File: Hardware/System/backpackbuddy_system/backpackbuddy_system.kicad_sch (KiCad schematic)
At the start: 27 parts, among them J1 PIR, J2 Ultrasonic 2, J3 Ultrasonic 1, J4 Left Vibration 1, J5 Left Vibration 2, J7 ESP8266, J8 Right Vibration 1, J9 Right Vibration 2, Q1 Q_NMOS_GSD, Q2 Q_NMOS_GSD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

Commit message: almost done
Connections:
- net microcontroller/PB3 is gone; now on net microcontroller/PD0: R10.1
- net +3V3: now also R14.1; no longer SW1.2
- net ESP RESET: now also R14.2; no longer R14.1
- net GND: now also SW1.2; no longer R14.2
- net microcontroller/PD0: no longer J3.3 (Pin_3)
- net microcontroller/PB2 renamed microcontroller/PB7
- net microcontroller/PB6 renamed microcontroller/PD3/TX
- new net microcontroller/PD0: J3.3 (Pin_3)
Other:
- sheet microcontroller ports: added PB7; removed PB2, PB3, PB6
- moved on the sheet: R14, SW1
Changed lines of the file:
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@@
     (stroke (width 0) (type default) (color 0 0 0 0))
   )
-  (wire (pts (xy 245.11 71.12) (xy 245.11 77.47))
+  (wire (pts (xy 245.11 73.66) (xy 245.11 77.47))
     (stroke (width 0) (type default) (color 0 0 0 0))
   )
@@
     (stroke (width 0) (type default) (color 0 0 0 0))
   )
-  (wire (pts (xy 245.11 62.23) (xy 245.11 60.96))
+  (wire (pts (xy 245.11 58.42) (xy 245.11 62.23))
     (stroke (width 0) (type default) (color 0 0 0 0))
   )
@@
     (pin "1")
   )
-  (symbol (lib_id "Switch:SW_Push") (at 245.11 55.88 90) (unit 1)
-    (in_bom yes) (on_board yes) (fields_autoplaced)
-    (property "Reference" "SW1" (id 0) (at 246.38 54.6099 90)
-      (effects (font (size 1.27 1.27)) (justify right))
-    )
-    (property "Value" "ESP8266 RESET" (id 1) (at 246.38 57.1499 90)
-      (effects (font (size 1.27 1.27)) (justify right))
-    )
-    (property "Footprint" "BackpackBuddyFootprintLibrary:RST_SW" (id 2) (at 240.03 55.88 0)
-      (effects (font (size 1.27 1.27)) hide)
-    )
-    (property "Datasheet" "https://www.nkkswitches.com/pdf/HP03-2.pdf" (id 3) (at 240.03 55.88 0)
-      (effects (font (size 1.27 1.27)) hide)
-    )
-    (property "MPN" "HP0315AFKP2-R" (id 4) (at 245.11 55.88 0)
-      (effects (font (size 1.27 1.27)) hide)
-    )
-    (property "Stock" "https://www.digikey.com/en/products/detail/nkk-switches/HP0315AFKP2-R/1242035" (id 5) (at 245.11 55.88 0)
+  (symbol (lib_id "Switch:SW_Push") (at 245.11 68.58 270) (unit 1)
+    (in_bom yes) (on_board yes) (fields_autoplaced)
+    (property "Reference" "SW1" (id 0) (at 248.92 67.3099 90)
+      (effects (font (size 1.27 1.27)) (justify left))
+    )
+    (property "Value" "ESP8266 RESET" (id 1) (at 248.92 69.8499 90)
+      (effects (font (size 1.27 1.27)) (justify left))
+    )
+    (property "Footprint" "BackpackBuddyFootprintLibrary:RST_SW" (id 2) (at 250.19 68.58 0)
+      (effects (font (size 1.27 1.27)) hide)
+    )
+    (property "Datasheet" "https://www.nkkswitches.com/pdf/HP03-2.pdf" (id 3) (at 250.19 68.58 0)
+      (effects (font (size 1.27 1.27)) hide)
+    )
+    (property "MPN" "HP0315AFKP2-R" (id 4) (at 245.11 68.58 0)
+      (effects (font (size 1.27 1.27)) hide)
+    )
+    (property "Stock" "https://www.digikey.com/en/products/detail/nkk-switches/HP0315AFKP2-R/1242035" (id 5) (at 245.11 68.58 0)
       (effects (font (size 1.27 1.27)) hide)
     )
@@
     (pin "1")
   )
-  (symbol (lib_id "Device:R") (at 245.11 67.31 0) (unit 1)
-    (in_bom yes) (on_board yes) (fields_autoplaced)
-    (property "Reference" "R14" (id 0) (at 247.65 66.0399 0)
-      (effects (font (size 1.27 1.27)) (justify left))
-    )
-    (property "Value" "10k" (id 1) (at 247.65 68.5799 0)
-      (effects (font (size 1.27 1.27)) (justify left))
-    )
-    (property "Footprint" "Resistor_SMD:R_0603_1608Metric_Pad0.98x0.95mm_HandSolder" (id 2) (at 243.332 67.31 90)
-      (effects (font (size 1.27 1.27)) hide)
-    )
-    (property "Datasheet" "~" (id 3) (at 245.11 67.31 0)
-      (effects (font (size 1.27 1.27)) hide)
-    )
-    (property "MPN" "RES 10K OHM 1% 1/10W 0603" (id 4) (at 245.11 67.31 0)
-      (effects (font (size 1.27 1.27)) hide)
-    )
-    (property "Stock" "https://www.digikey.com/en/products/detail/vishay-dale/CRCW060310K0FKECC/12744930?utm_adgroup=Resistors&utm_source=google&utm_medium=cpc&utm_campaign=Shopping_Supplier_Vishay&utm_term=&utm_content=Resistors" (id 5) (at 245.11 67.31 0)
+  (symbol (lib_id "Device:R") (at 245.11 54.61 0) (unit 1)
+    (in_bom yes) (on_board yes) (fields_autoplaced)
+    (property "Reference" "R14" (id 0) (at 247.65 53.3399 0)
+      (effects (font (size 1.27 1.27)) (justify left))
+    )
+    (property "Value" "10k" (id 1) (at 247.65 55.8799 0)
+      (effects (font (size 1.27 1.27)) (justify left))
+    )
+    (property "Footprint" "Resistor_SMD:R_0603_1608Metric_Pad0.98x0.95mm_HandSolder" (id 2) (at 243.332 54.61 90)
+      (effects (font (size 1.27 1.27)) hide)
+    )
+    (property "Datasheet" "~" (id 3) (at 245.11 54.61 0)
+      (effects (font (size 1.27 1.27)) hide)
+    )
+    (property "MPN" "RES 10K OHM 1% 1/10W 0603" (id 4) (at 245.11 54.61 0)
+      (effects (font (size 1.27 1.27)) hide)
+    )
+    (property "Stock" "https://www.digikey.com/en/products/detail/vishay-dale/CRCW060310K0FKECC/12744930?utm_adgroup=Resistors&utm_source=google&utm_medium=cpc&utm_campaign=Shopping_Supplier_Vishay&utm_term=&utm_content=Resistors" (id 5) (at 245.11 54.61 0)
       (effects (font (size 1.27 1.27)) hide)
     )
@@
       (effects (font (size 1.27 1.27)) (justify right))
     )
-    (pin "PB2" bidirectional (at 132.08 43.18 180)
+    (pin "PB7" bidirectional (at 132.08 43.18 180)
       (effects (font (size 1.27 1.27)) (justify left))
     )
@@
       (effects (font (size 1.27 1.27)) (justify right))
     )
-    (pin "PB3" bidirectional (at 132.08 58.42 180)
+    (pin "PD0" bidirectional (at 132.08 58.42 180)
       (effects (font (size 1.27 1.27)) (justify left))
     )
@@
       (effects (font (size 1.27 1.27)) (justify left))
     )
-    (pin "PB6" bidirectional (at 132.08 66.04 180)
+    (pin "PD3{slash}TX" bidirectional (at 132.08 66.04 180)
       (effects (font (size 1.27 1.27)) (justify left))
     )
@@
       (reference "C24") (unit 1) (value "10uF") (footprint "Capacitor_SMD:C_0805_2012Metric_Pad1.18x1.45mm_HandSolder")
     )
-    (path "/b75bd9b9-3a6b-4766-98aa-3c30f703f2e0/a43d5dce-b543-4961-b95c-4a978a724427"
-      (reference "C25") (unit 1) (value "10uF") (footprint "Capacitor_SMD:C_0805_2012Metric_Pad1.18x1.45mm_HandSolder")
-    )
     (path "/af61f2eb-3376-4189-8310-620a433ef8ef/1d374c9e-2897-4c07-9d24-38daf6ec840d"

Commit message: first draft done :))) still errors but thats because i was too lazy to do no connects as of rn
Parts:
- removed D9: Blue, LED_SMD:LED_0603_1608Metric_Pad1.05x0.95mm_HandSolder, symbol Device:LED
- added JP2: PP Short, Jumper:SolderJumper-2_P1.3mm_Open_RoundedPad1.0x1.5mm, symbol Jumper:SolderJumper_2_Open
- added R15, R16: 1k, Resistor_SMD:R_0603_1608Metric_Pad0.98x0.95mm_HandSolder, symbol Device:R
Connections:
- net microcontroller/PB1 is gone; now on net microcontroller/PB5: J7.5 (Pin_5)
- net microcontroller/PD2/RX is gone; now on net ESP_RX: J7.7 (Pin_7)
- net microcontroller/PD3/TX is gone; now on net microcontroller/PD3/TX: J7.2 (Pin_2)
- net microcontroller/PD5 is gone; now on net microcontroller/PD1: J2.2 (Pin_2)
- net GND: now also R16.2
- net microcontroller/PB4: now also Q1.1 (G); no longer R11.1
- net microcontroller/PB5: no longer R12.1
- net microcontroller/PD0: now also J2.3 (Pin_3); no longer J3.3 (Pin_3)
- net microcontroller/PD1: no longer J3.2 (Pin_2)
- net microcontroller/PD3/TX: no longer R13.1
- net microcontroller/PD4: now also R13.1; no longer J2.3 (Pin_3)
- net microcontroller/PD6: now also J3.3 (Pin_3); no longer TP7.1
- net microcontroller/PD7: now also J3.2 (Pin_2); no longer TP8.1
- net microcontroller/PF5: now also R12.1; no longer Q1.1 (G)
- net ESP_RX: now reaches R10.2
- net ESP_RX: now also JP2.1 (A), R15.1
- net microcontroller/PB0: no longer names the net of J7.3 (Pin_3)
- net microcontroller/PD0 renamed PD2/RX
- net PD2/RX: now also JP2.2 (B)
- net microcontroller/PF6 renamed microcontroller/PB6
- new net: R15.2, R16.1
- new net Raspberry Pi/GPIO17: TP7.1
- new net Raspberry Pi/GPIO27: TP8.1
- new net microcontroller/PF7: R11.1
- no-connect marks 0 -> 1
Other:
- sheet Raspberry Pi ports: added GPIO17, GPIO22, GPIO27; removed none
- sheet microcontroller ports: added PB6, PC6, PC7, PF7; removed PB0, PB1, PD5
- moved on the sheet: R14, SW1, TP7

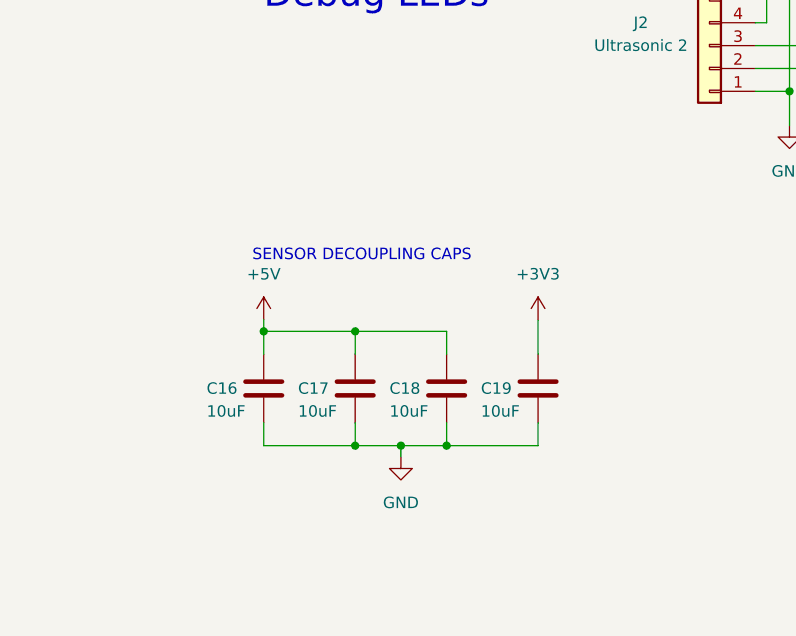
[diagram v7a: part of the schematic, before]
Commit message: silkscreen done
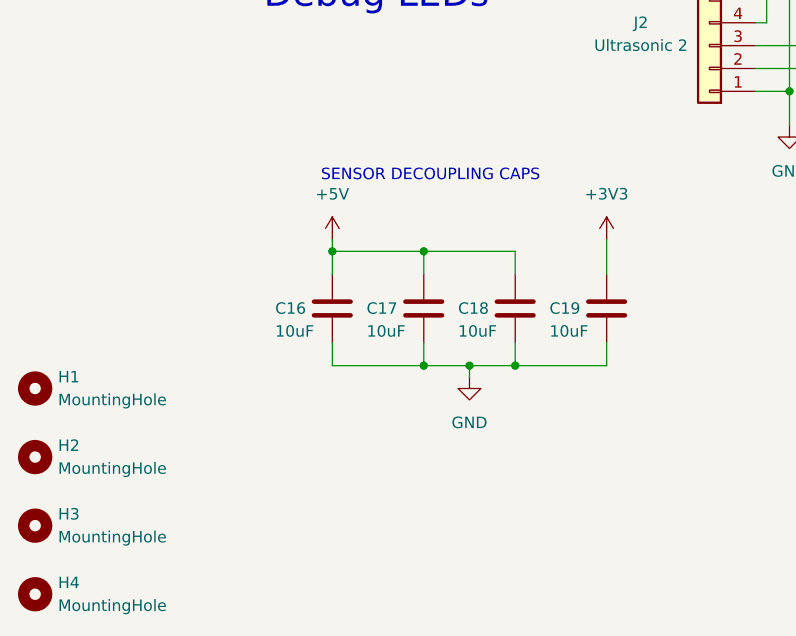
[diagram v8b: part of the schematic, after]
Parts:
- added H1, H2, H3, H4: MountingHole, symbol Mechanical:MountingHole
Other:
- moved on the sheet: C16, C17, C18, C19
